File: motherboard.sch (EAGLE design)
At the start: 198 parts, among them IC1 LM2576, IC10 TUSB2046B, IC12 LM50, IC13 LM50, IC2 74LS595D, IC3 74LS595D, IC4 IC_FT230X-SSOP-16, IC5 VN5772AK, IC6 VN5772AK, IC7 VN5772AK, IC8 VN5772AK, IC9 VN5772AK, SW1 FSMSM, U2 NCP4625, U3 ATMEGA168, Y1 16Mhz, Y2 6MHz

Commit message: laying out protection diodes
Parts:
- added C44, C45: 1000uF, adafruit:CPOL-US153CLV-0807
- added F4, F9: (no value), special:FUSE2P
- added JP11, JP12: (no value), sparkfun:M023.5MM
- added Q5, Q6: (no value), adafruit:MOSFET-NREFLOW
- added R26, R36, R6, R7, R9: 70, adafruit:R-US_R1206
- added U$19, U$20: TVS, sparkfun:TVS
- R11: value (none) -> 1.5k
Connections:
- new net N$72: JP11.2, Q5.D
- new net N$73: JP12.2, Q6.D
- new net N$74: C45.+, F9.1A, JP12.1, U$20.2
- new net N$75: C44.+, F4.1A, JP11.1, U$19.2
- new net N$76: IC5.SENSE, R6.2
- new net N$77: IC7.SENSE, R7.2
- new net N$78: IC6.SENSE, R9.2
- new net N$79: IC9.SENSE, R36.2
- new net N$80: IC8.SENSE, R26.2
- net +12V: now also F4.2A, F9.2A
- net 0SENSE: now also R6.1; no longer IC5.SENSE
- net 1SENSE: now also R7.1; no longer IC7.SENSE
- net 2SENSE: now also R9.1; no longer IC6.SENSE
- net 3SENSE: now also R36.1; no longer IC9.SENSE
- net 4SENSE: now also R26.1; no longer IC8.SENSE
- net GND: now also C44.-, C45.-, Q5.S, Q6.S, U$19.1, U$20.1
- net SW4: now also Q5.G
- net SW5: now also Q6.G
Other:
- moved on the sheet: C53, C54, C55, C56, F5, F6, F7, F8, JP14, JP15, JP16, JP17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

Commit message: laying out components
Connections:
- net SW3: now also R54.1
- net SW4: no longer R54.1
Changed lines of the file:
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@@
 <grid distance="0.1" unitdist="inch" unit="inch" style="lines" multiple="1" display="no" altdistance="0.01" altunitdist="inch" altunit="inch"/>
 <layers>
-<layer number="1" name="Top" color="4" fill="1" visible="no" active="no"/>
-<layer number="2" name="Route2" color="1" fill="3" visible="no" active="no"/>
-<layer number="3" name="Route3" color="4" fill="3" visible="no" active="no"/>
-<layer number="4" name="Route4" color="1" fill="4" visible="no" active="no"/>
-<layer number="5" name="Route5" color="4" fill="4" visible="no" active="no"/>
-<layer number="6" name="Route6" color="1" fill="8" visible="no" active="no"/>
-<layer number="7" name="Route7" color="4" fill="8" visible="no" active="no"/>
-<layer number="8" name="Route8" color="1" fill="2" visible="no" active="no"/>
-<layer number="9" name="Route9" color="4" fill="2" visible="no" active="no"/>
-<layer number="10" name="Route10" color="1" fill="7" visible="no" active="no"/>
-<layer number="11" name="Route11" color="4" fill="7" visible="no" active="no"/>
-<layer number="12" name="Route12" color="1" fill="5" visible="no" active="no"/>
-<layer number="13" name="Route13" color="4" fill="5" visible="no" active="no"/>
-<layer number="14" name="Route14" color="1" fill="6" visible="no" active="no"/>
-<layer number="15" name="Route15" color="4" fill="6" visible="no" active="no"/>
-<layer number="16" name="Bottom" color="1" fill="1" visible="no" active="no"/>
-<layer number="17" name="Pads" color="2" fill="1" visible="no" active="no"/>
-<layer number="18" name="Vias" color="2" fill="1" visible="no" active="no"/>
-<layer number="19" name="Unrouted" color="6" fill="1" visible="no" active="no"/>
-<layer number="20" name="Dimension" color="15" fill="1" visible="no" active="no"/>
-<layer number="21" name="tPlace" color="7" fill="1" visible="no" active="no"/>
-<layer number="22" name="bPlace" color="7" fill="1" visible="no" active="no"/>
-<layer number="23" name="tOrigins" color="15" fill="1" visible="no" active="no"/>
-<layer number="24" name="bOrigins" color="15" fill="1" visible="no" active="no"/>
-<layer number="25" name="tNames" color="7" fill="1" visible="no" active="no"/>
-<layer number="26" name="bNames" color="7" fill="1" visible="no" active="no"/>
-<layer number="27" name="tValues" color="7" fill="1" visible="no" active="no"/>
-<layer number="28" name="bValues" color="7" fill="1" visible="no" active="no"/>
+<layer number="1" name="Top" color="4" fill="1" visible="yes" active="no"/>
+<layer number="2" name="Route2" color="1" fill="3" visible="yes" active="no"/>
+<layer number="3" name="Route3" color="4" fill="3" visible="yes" active="no"/>
+<layer number="4" name="Route4" color="1" fill="4" visible="yes" active="no"/>
+<layer number="5" name="Route5" color="4" fill="4" visible="yes" active="no"/>
+<layer number="6" name="Route6" color="1" fill="8" visible="yes" active="no"/>
+<layer number="7" name="Route7" color="4" fill="8" visible="yes" active="no"/>
+<layer number="8" name="Route8" color="1" fill="2" visible="yes" active="no"/>
+<layer number="9" name="Route9" color="4" fill="2" visible="yes" active="no"/>
+<layer number="10" name="Route10" color="1" fill="7" visible="yes" active="no"/>
+<layer number="11" name="Route11" color="4" fill="7" visible="yes" active="no"/>
+<layer number="12" name="Route12" color="1" fill="5" visible="yes" active="no"/>
+<layer number="13" name="Route13" color="4" fill="5" visible="yes" active="no"/>
+<layer number="14" name="Route14" color="1" fill="6" visible="yes" active="no"/>
+<layer number="15" name="Route15" color="4" fill="6" visible="yes" active="no"/>
+<layer number="16" name="Bottom" color="1" fill="1" visible="yes" active="no"/>
+<layer number="17" name="Pads" color="2" fill="1" visible="yes" active="no"/>
+<layer number="18" name="Vias" color="2" fill="1" visible="yes" active="no"/>
+<layer number="19" name="Unrouted" color="6" fill="1" visible="yes" active="no"/>
+<layer number="20" name="Dimension" color="15" fill="1" visible="yes" active="no"/>
+<layer number="21" name="tPlace" color="7" fill="1" visible="yes" active="no"/>
+<layer number="22" name="bPlace" color="7" fill="1" visible="yes" active="no"/>
+<layer number="23" name="tOrigins" color="15" fill="1" visible="yes" active="no"/>
+<layer number="24" name="bOrigins" color="15" fill="1" visible="yes" active="no"/>
+<layer number="25" name="tNames" color="7" fill="1" visible="yes" active="no"/>
+<layer number="26" name="bNames" color="7" fill="1" visible="yes" active="no"/>
+<layer number="27" name="tValues" color="7" fill="1" visible="yes" active="no"/>
+<layer number="28" name="bValues" color="7" fill="1" visible="yes" active="no"/>
 <layer number="29" name="tStop" color="7" fill="3" visible="no" active="no"/>
 <layer number="30" name="bStop" color="7" fill="6" visible="no" active="no"/>
@@
 <layer number="35" name="tGlue" color="7" fill="4" visible="no" active="no"/>
 <layer number="36" name="bGlue" color="7" fill="5" visible="no" active="no"/>
-<layer number="37" name="tTest" color="7" fill="1" visible="no" active="no"/>
-<layer number="38" name="bTest" color="7" fill="1" visible="no" active="no"/>
+<layer number="37" name="tTest" color="7" fill="1" visible="yes" active="no"/>
+<layer number="38" name="bTest" color="7" fill="1" visible="yes" active="no"/>
 <layer number="39" name="tKeepout" color="4" fill="11" visible="no" active="no"/>
 <layer number="40" name="bKeepout" color="1" fill="11" visible="no" active="no"/>
@@
 <layer number="44" name="Drills" color="7" fill="1" visible="no" active="no"/>
 <layer number="45" name="Holes" color="7" fill="1" visible="no" active="no"/>
-<layer number="46" name="Milling" color="3" fill="1" visible="no" active="no"/>
-<layer number="47" name="Measures" color="7" fill="1" visible="no" active="no"/>
-<layer number="48" name="Document" color="7" fill="1" visible="no" active="no"/>
-<layer number="49" name="Reference" color="7" fill="1" visible="no" active="no"/>
-<layer number="50" name="dxf" color="7" fill="1" visible="no" active="no"/>
-<layer number="51" name="tDocu" color="6" fill="1" visible="no" active="no"/>
-<layer number="52" name="bDocu" color="7" fill="1" visible="no" active="no"/>
-<layer number="53" name="tGND_GNDA" color="7" fill="9" visible="no" active="no"/>
-<layer number="54" name="bGND_GNDA" color="1" fill="9" visible="no" active="no"/>
-<layer number="56" name="wert" color="7" fill="1" visible="no" active="no"/>
-<layer number="57" name="tCAD" color="7" fill="1" visible="no" active="no"/>
+<layer number="46" name="Milling" color="3" fill="1" visible="yes" active="no"/>
+<layer number="47" name="Measures" color="7" fill="1" visible="yes" active="no"/>
+<layer number="48" name="Document" color="7" fill="1" visible="yes" active="no"/>
+<layer number="49" name="Reference" color="7" fill="1" visible="yes" active="no"/>
+<layer number="50" name="dxf" color="7" fill="1" visible="yes" active="no"/>
+<layer number="51" name="tDocu" color="7" fill="1" visible="yes" active="no"/>
+<layer number="52" name="bDocu" color="7" fill="1" visible="yes" active="no"/>
+<layer number="53" name="tGND_GNDA" color="7" fill="9" visible="yes" active="no"/>
+<layer number="54" name="bGND_GNDA" color="1" fill="9" visible="yes" active="no"/>
+<layer number="56" name="wert" color="7" fill="1" visible="yes" active="no"/>
+<layer number="57" name="tCAD" color="7" fill="1" visible="yes" active="no"/>
 <layer number="91" name="Nets" color="2" fill="1" visible="yes" active="yes"/>
 <layer number="92" name="Busses" color="1" fill="1" visible="yes" active="yes"/>
@@
 <label x="353.06" y="177.8" size="1.778" layer="95"/>
 </segment>
+<segment>
+<label x="264.16" y="116.84" size="1.778" layer="95"/>
+<pinref part="R54" gate="G$1" pin="1"/>
+<wire x1="261.62" y1="116.84" x2="271.78" y2="116.84" width="0.1524" layer="91"/>
+</segment>
 </net>
 <net name="SW2" class="0">
@@
 </segment>
 <segment>
-<label x="264.16" y="116.84" size="1.778" layer="95"/>
-<pinref part="R54" gate="G$1" pin="1"/>
-<wire x1="261.62" y1="116.84" x2="271.78" y2="116.84" width="0.1524" layer="91"/>
-</segment>
-<segment>

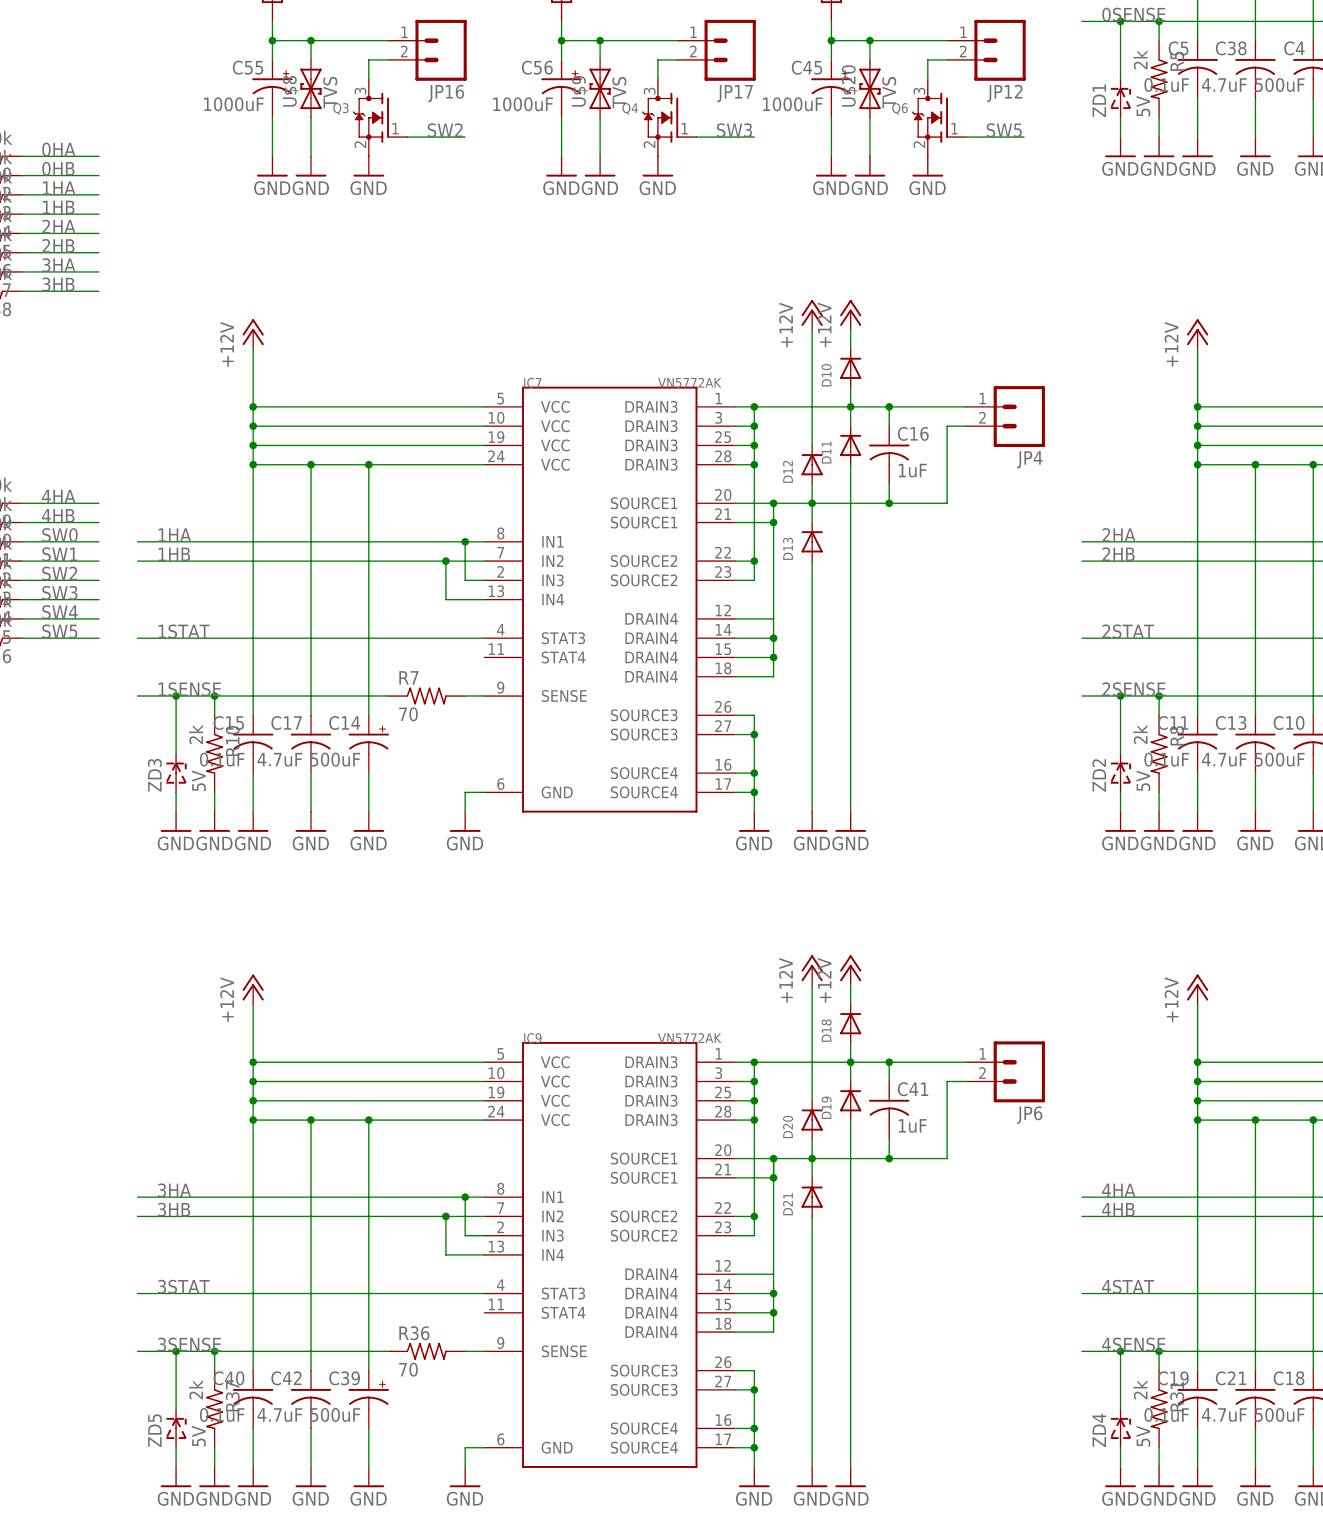
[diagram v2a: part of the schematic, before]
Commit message: changing h bridge layout
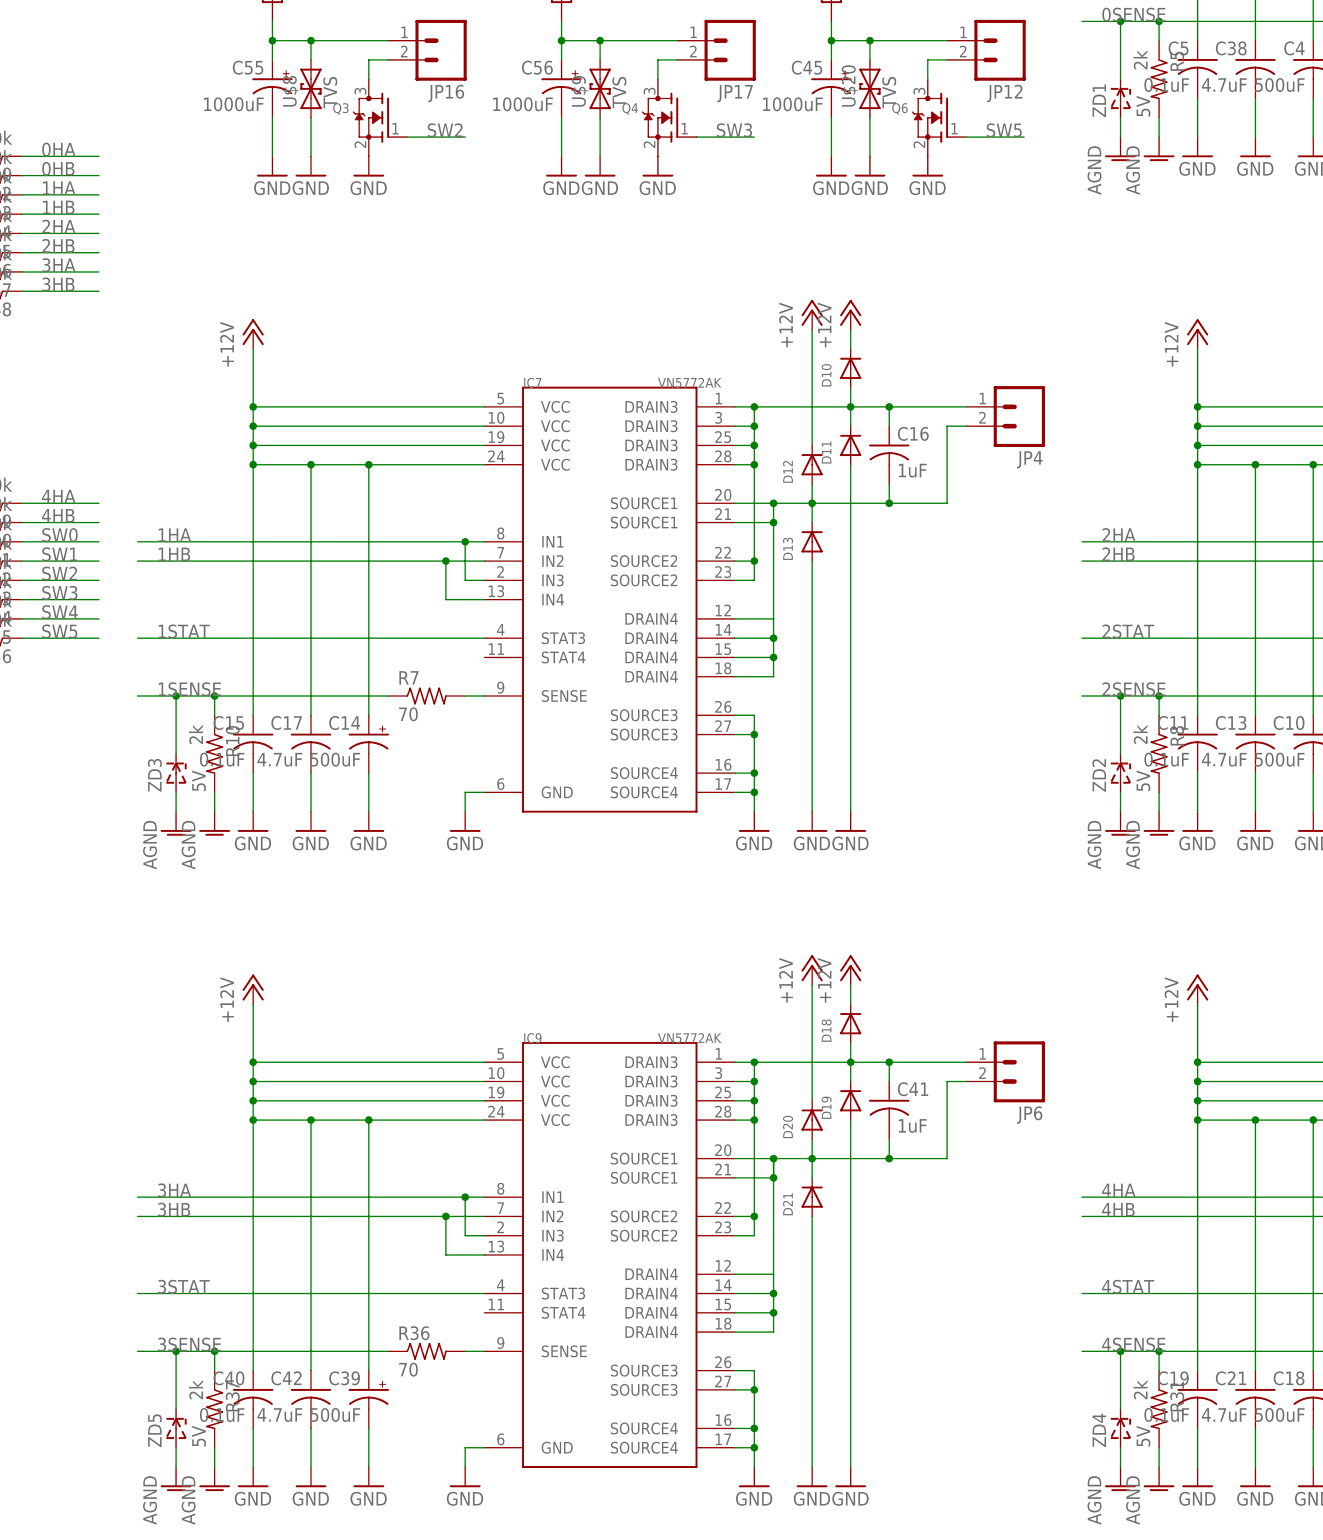
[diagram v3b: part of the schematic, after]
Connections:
- net AGND: now also R10.2, R31.2, R37.2, R5.2, R8.2, ZD1.A, ZD2.A, ZD3.A, ZD4.A, ZD5.A
- net GND: no longer R10.2, R31.2, R37.2, R5.2, R8.2, ZD1.A, ZD2.A, ZD3.A, ZD4.A, ZD5.A

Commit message: layed out hbridges, MCU, new fuses
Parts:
- removed C44, C45, C56: 1000uF, adafruit:CPOL-US153CLV-0807
- removed F5, F6, F7: (no value), special:FUSE2P
- removed JP10, JP9: (no value), sparkfun:M04SCREW
- removed JP7: (no value), sparkfun:M023.5MM
- removed L1: 100uH, sparkfun:INDUCTOR1206H*
- removed Q4, Q5, Q6: (no value), adafruit:MOSFET-NREFLOW
- removed U$19, U$20, U$9: TVS, sparkfun:TVS
- added JP13: (no value), sparkfun:M04SCREW
- added L18: 100uH, sparkfun:INDUCTORPWR
- F4, F8, F9: value (none) -> 3557-2; device special:FUSE2P -> rov_club:3557-2
- JP11, JP17: device sparkfun:M023.5MM -> sparkfun:M04SCREW
- JP12: device sparkfun:M023.5MM -> sparkfun:M03PTH
- JP8: device sparkfun:M04SCREW -> sparkfun:M023.5MM
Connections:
- removed net N$20: C56.+, F8.1A, JP17.1, U$9.2
- removed net N$57: JP17.2, Q4.D
- removed net N$72: JP11.2, Q5.D
- removed net N$73: JP12.2, Q6.D
- removed net N$74: C45.+, F9.1A, JP12.1, U$20.2
- removed net N$75: C44.+, F4.1A, JP11.1, U$19.2
- net +12V: now also F4.2B, F8.2B, F9.2B; no longer F5.2A, F6.2A, F7.2A
- net +5V: now also L18.2; no longer L1.2
- net GND: now also JP11.1, JP13.1, JP17.1; no longer C44.-, C45.-, C56.-, JP10.4, JP8.4, JP9.4, Q4.S, Q5.S, Q6.S, U$19.1, U$20.1, U$9.1
- net N$1: now also L18.1; no longer L1.1
- net N$21: now also JP17.2; no longer JP10.3
- net N$24: now also JP17.3; no longer JP10.2
- net N$25: now also JP13.3; no longer JP9.2
- net N$32: now also JP13.2; no longer JP9.3
- net N$33: now also JP11.3; no longer JP8.2
- net N$34: now also JP11.2; no longer JP8.3
- net N$35: now also JP17.4; no longer JP10.1
- net N$36: now also JP13.4; no longer JP9.1
- net N$37: now also JP11.4; no longer JP8.1
- net N$43: now also JP14.1; no longer JP14.2
- net N$44: now also JP8.1; no longer JP7.1
- net N$45: now also JP8.2; no longer JP7.2
- net N$47: now also JP15.1; no longer JP15.2
- net N$48: now also JP16.1; no longer JP16.2
- net N$50: now also F9.1A, F9.1B, JP16.2; no longer F7.1A, JP16.1
- net N$54: now also F8.1A, F8.1B, JP15.2; no longer F6.1A, JP15.1
- net N$55: now also F4.1A, F4.1B, JP14.2; no longer F5.1A, JP14.1
- net SW3: now also JP12.1; no longer Q4.G
- net SW4: now also JP12.2; no longer Q5.G
- net SW5: now also JP12.3; no longer Q6.G
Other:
- moved on the sheet: F4, F8, F9, JP14, JP15, JP16

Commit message: positioned all but mcu
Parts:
- removed R40, R42, R43, R44, R45, R46, R47, R48, R49, R50, R51, R52, R53, R54, R55, R56: 10k, adafruit:R-US_R1206
- added R41, R57: 10k, resistor-bourns:2NBS16-8E
- D10, D11, D12, D13, D14, D15, D16, D17, D18, D19, D2, D20, D21, D3, D4, D5, D6, D7, D8, D9: device adafruit:DIODESMA -> adafruit:DIODESOD-123
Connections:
- net 0HA: now also R41C.1; no longer R40.1
- net 0HB: now also R41A.1; no longer R42.1
- net 1HA: now also R41B.1; no longer R43.1
- net 1HB: now also R41D.1; no longer R44.1
- net 2HA: now also R41E.1; no longer R45.1
- net 2HB: now also R41F.1; no longer R46.1
- net 3HA: now also R41G.1; no longer R47.1
- net 3HB: now also R41H.1; no longer R48.1
- net 4HA: now also R57C.1; no longer R49.1
- net 4HB: now also R57A.1; no longer R50.1
- net N$10: now also JP5.1; no longer JP5.2
- net N$11: now also JP5.2; no longer JP5.1
- net N$12: now also JP6.1; no longer JP6.2
- net N$13: now also JP2.1; no longer JP2.2
- net N$14: now also JP6.2; no longer JP6.1
- net N$15: now also R57H.2; no longer R56.2
- net N$17: now also R57G.2; no longer R55.2
- net N$18: now also R57F.2; no longer R54.2
- net N$3: now also JP3.1; no longer JP3.2
- net N$5: now also JP3.2; no longer JP3.1
- net N$56: now also R57E.2; no longer R53.2
- net N$59: now also JP2.2; no longer JP2.1
- net N$60: now also R57D.2; no longer R52.2
- net N$61: now also R57B.2; no longer R51.2
- net N$62: now also R57A.2; no longer R50.2
- net N$63: now also R57C.2; no longer R49.2
- net N$64: now also R41H.2; no longer R48.2
- net N$65: now also R41G.2; no longer R47.2
- net N$66: now also R41F.2; no longer R46.2
- net N$67: now also R41E.2; no longer R45.2
- net N$68: now also R41D.2; no longer R44.2
- net N$69: now also R41B.2; no longer R43.2
- net N$70: now also R41A.2; no longer R42.2
- net N$71: now also R41C.2; no longer R40.2
- net N$8: now also JP4.1; no longer JP4.2
- net N$9: now also JP4.2; no longer JP4.1
- net SW0: now also R57B.1; no longer R51.1
- net SW1: now also R57D.1; no longer R52.1
- net SW2: now also R57E.1; no longer R53.1
- net SW3: now also R57F.1; no longer R54.1
- net SW4: now also R57G.1; no longer R55.1
- net SW5: now also R57H.1; no longer R56.1
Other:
- moved on the sheet: JP2, JP3, JP4, JP5, JP6
